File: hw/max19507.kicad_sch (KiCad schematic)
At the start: 33 parts, among them U9 MAX19517

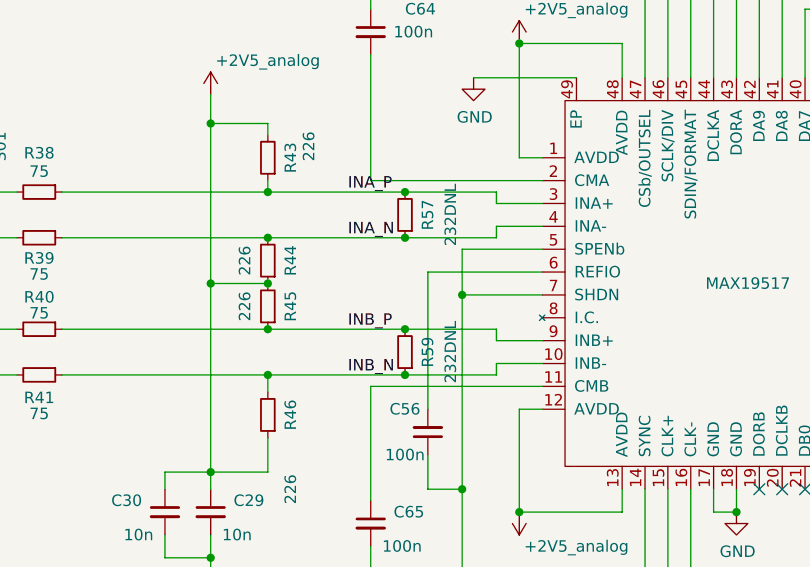
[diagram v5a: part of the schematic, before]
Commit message: Added (optional) connection from PLL output 4 to ulpi refclock.
Could spare the crystal oscillator...
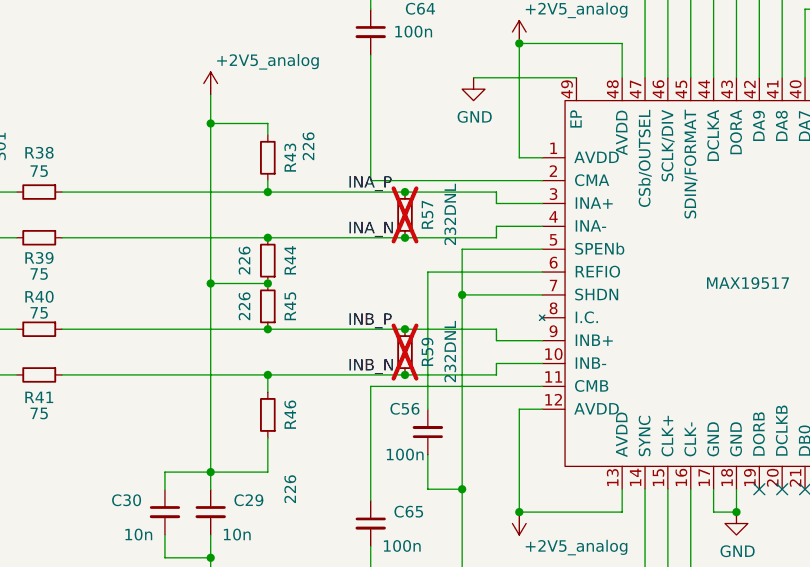
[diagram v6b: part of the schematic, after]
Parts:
- R57, R59: now not fitted
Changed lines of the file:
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@@
   )
   (symbol (lib_id "Device:R_Small") (at 186.69 78.74 180) (unit 1)
-    (in_bom yes) (on_board yes) (dnp no)
+    (in_bom yes) (on_board yes) (dnp yes)
     (property "Reference" "R57" (at 189.23 78.74 90)
       (effects (font (size 1.27 1.27)))
@@
   )
   (symbol (lib_id "Device:R_Small") (at 186.69 93.98 180) (unit 1)
-    (in_bom yes) (on_board yes) (dnp no)
+    (in_bom yes) (on_board yes) (dnp yes)
     (property "Reference" "R59" (at 189.23 93.98 90)
       (effects (font (size 1.27 1.27)))

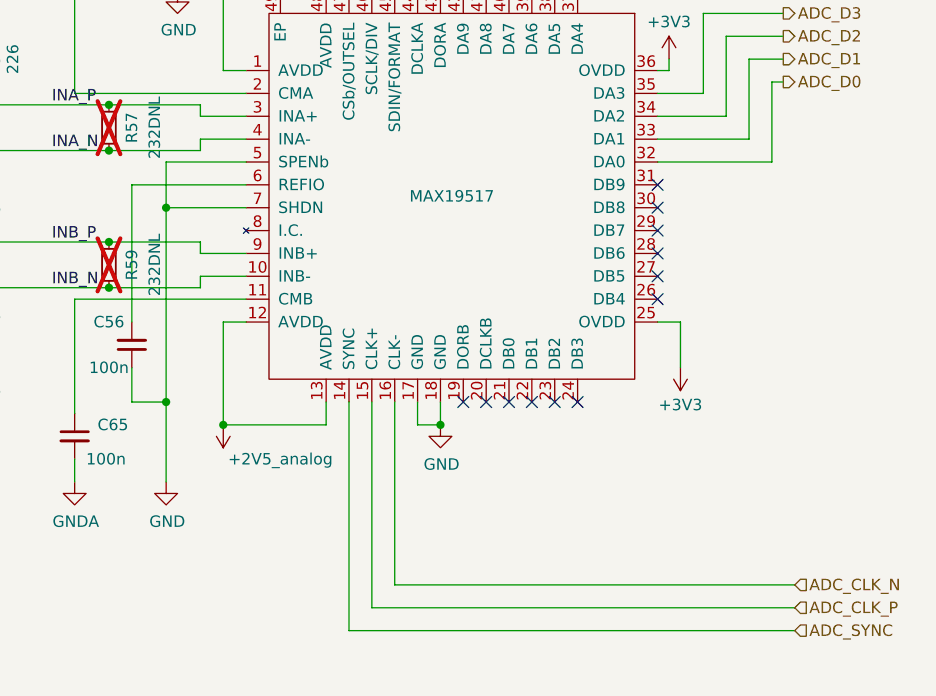
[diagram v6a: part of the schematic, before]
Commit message: Modified DAC resistors/range; connect + pull-up ADC SHDN
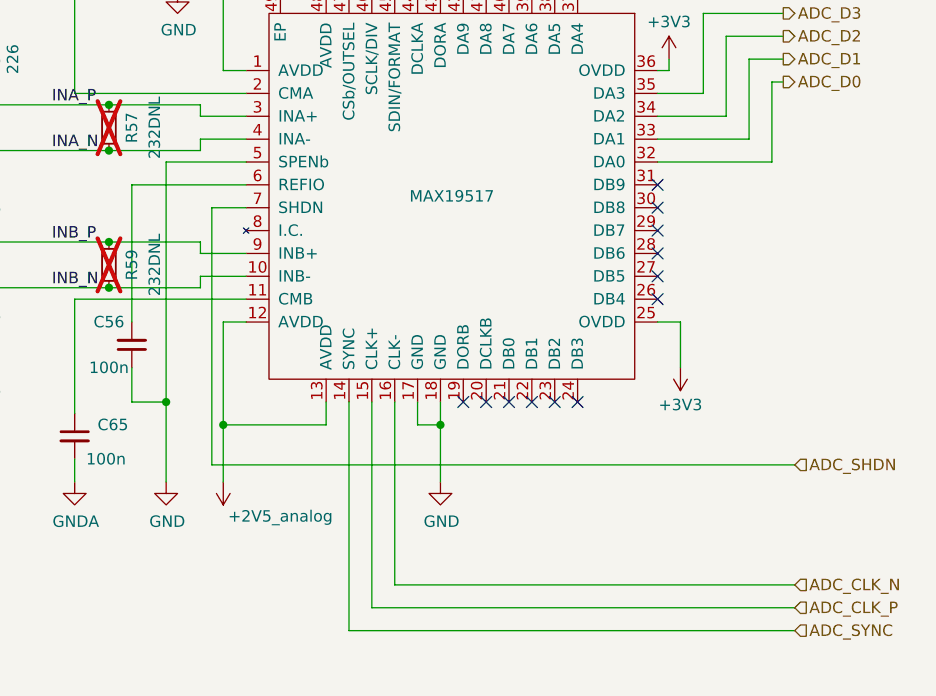
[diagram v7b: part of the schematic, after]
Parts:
- R57, R59: now left out of the parts list
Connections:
- net GND: no longer U9.7 (SHDN)
- new net ADC_SHDN: U9.7 (SHDN)
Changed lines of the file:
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@@
   (junction (at 186.69 81.28) (diameter 0) (color 0 0 0 0)
-  )
-  (junction (at 193.04 87.63) (diameter 0) (color 0 0 0 0)
   )
   (no_connect (at 247.65 87.63))
@@
     (stroke (width 0) (type default))
   )
-  (wire (pts (xy 193.04 82.55) (xy 193.04 87.63))
+  (wire (pts (xy 193.04 82.55) (xy 193.04 109.22))
     (stroke (width 0) (type default))
   )
@@
     (stroke (width 0) (type default))
   )
+  (wire (pts (xy 198.12 116.205) (xy 262.89 116.205))
+    (stroke (width 0) (type default))
+  )
   (wire (pts (xy 261.62 68.58) (xy 255.27 68.58))
     (stroke (width 0) (type default))
@@
     (stroke (width 0) (type default))
   )
+  (wire (pts (xy 198.12 87.63) (xy 198.12 116.205))
+    (stroke (width 0) (type default))
+  )
   (wire (pts (xy 165.1 86.36) (xy 171.45 86.36))
     (stroke (width 0) (type default))
@@
     (stroke (width 0) (type default))
   )
+  (wire (pts (xy 223.52 118.11) (xy 223.52 111.76))
+    (stroke (width 0) (type default))
+  )
   (wire (pts (xy 228.6 53.34) (xy 261.62 53.34))
     (stroke (width 0) (type default))
@@
     (stroke (width 0) (type default))
   )
-  (wire (pts (xy 193.04 87.63) (xy 193.04 109.22))
-    (stroke (width 0) (type default))
-  )
   (wire (pts (xy 148.59 96.52) (xy 171.45 96.52))
     (stroke (width 0) (type default))
@@
     (stroke (width 0) (type default))
   )
+  (wire (pts (xy 201.93 87.63) (xy 198.12 87.63))
+    (stroke (width 0) (type default))
+  )
   (wire (pts (xy 171.45 91.44) (xy 186.69 91.44))
     (stroke (width 0) (type default))
@@
     (stroke (width 0) (type default))
   )
+  (wire (pts (xy 199.39 118.11) (xy 199.39 111.76))
+    (stroke (width 0) (type default))
+  )
   (wire (pts (xy 215.9 158.75) (xy 215.9 160.02))
     (stroke (width 0) (type default))
@@
   )
   (wire (pts (xy 127 91.44) (xy 137.16 91.44))
-    (stroke (width 0) (type default))
-  )
-  (wire (pts (xy 201.93 87.63) (xy 193.04 87.63))
     (stroke (width 0) (type default))
   )
@@
     (effects (font (size 1.27 1.27)) (justify left))
   )
+  (hierarchical_label "ADC_SHDN" (shape input) (at 262.89 116.205 0) (fields_autoplaced)
+    (effects (font (size 1.27 1.27)) (justify left))
+  )
   (hierarchical_label "ADC_D4" (shape output) (at 261.62 63.5 0) (fields_autoplaced)
     (effects (font (size 1.27 1.27)) (justify left))
@@
   )
   (symbol (lib_id "Device:R_Small") (at 186.69 78.74 180) (unit 1)
-    (in_bom yes) (on_board yes) (dnp yes)
+    (in_bom no) (on_board yes) (dnp yes)
     (property "Reference" "R57" (at 189.23 78.74 90)
       (effects (font (size 1.27 1.27)))
@@
   )
   (symbol (lib_id "Device:R_Small") (at 186.69 93.98 180) (unit 1)
-    (in_bom yes) (on_board yes) (dnp yes)
+    (in_bom no) (on_board yes) (dnp yes)
     (property "Reference" "R59" (at 189.23 93.98 90)
       (effects (font (size 1.27 1.27)))
@@
     )
   )
-  (symbol (lib_id "power:GND") (at 223.52 111.76 0) (unit 1)
-    (in_bom yes) (on_board yes) (dnp no)
-    (property "Reference" "#PWR0142" (at 223.52 118.11 0)
-      (effects (font (size 1.27 1.27)) hide)
-    )
-    (property "Value" "GND" (at 223.647 116.1542 0)
-      (effects (font (size 1.27 1.27)))
-    )
-    (property "Footprint" "" (at 223.52 111.76 0)
-      (effects (font (size 1.27 1.27)) hide)
-    )
-    (property "Datasheet" "" (at 223.52 111.76 0)
+  (symbol (lib_id "power:GND") (at 223.52 118.11 0) (unit 1)
+    (in_bom yes) (on_board yes) (dnp no)
+    (property "Reference" "#PWR0142" (at 223.52 124.46 0)
+      (effects (font (size 1.27 1.27)) hide)
+    )
+    (property "Value" "GND" (at 223.647 122.5042 0)
+      (effects (font (size 1.27 1.27)))
+    )
+    (property "Footprint" "" (at 223.52 118.11 0)
+      (effects (font (size 1.27 1.27)) hide)
+    )
+    (property "Datasheet" "" (at 223.52 118.11 0)
       (effects (font (size 1.27 1.27)) hide)
     )
@@
     )
   )
-  (symbol (lib_id "fmc:+2V5_analog") (at 199.39 111.76 0) (mirror x) (unit 1)
-    (in_bom yes) (on_board yes) (dnp no)
-    (property "Reference" "#PWR089" (at 199.39 107.95 0)
-      (effects (font (size 1.27 1.27)) hide)
-    )
-    (property "Value" "+2V5_analog" (at 205.74 115.57 0)
-      (effects (font (size 1.27 1.27)))
-    )
-    (property "Footprint" "" (at 199.39 111.76 0)
-      (effects (font (size 1.27 1.27)) hide)
-    )
-    (property "Datasheet" "" (at 199.39 111.76 0)
-      (effects (font (size 1.27 1.27)) hide)
-    )
+  (symbol (lib_id "fmc:+2V5_analog") (at 199.39 118.11 0) (mirror x) (unit 1)
+    (in_bom yes) (on_board yes) (dnp no)
+    (property "Reference" "#PWR089" (at 199.39 114.3 0)
+      (effects (font (size 1.27 1.27)) hide)
+    )
+    (property "Value" "+2V5_analog" (at 205.74 121.92 0)
+      (effects (font (size 1.27 1.27)))
+    )
+    (property "Footprint" "" (at 199.39 118.11 0)
+      (effects (font (size 1.27 1.27)) hide)
+    )
+    (property "Datasheet" "" (at 199.39 118.11 0)
+      (effects (font (size 1.27 1.27)) hide)
+    )
